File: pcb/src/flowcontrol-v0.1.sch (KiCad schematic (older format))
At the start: 30 parts, among them J1 Fan 1, J2 Fan 2, J3 Temp Sensor (10k Thermistor), J4 Temp Sensor (10k Thermistor), J5 Internal USB, J6 Molex 4 Pin, J7 4 Pin DRGB LED, SW1 K2-1102SP-C4SC-04, U1 PICO_RP2040, U2 CH340G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

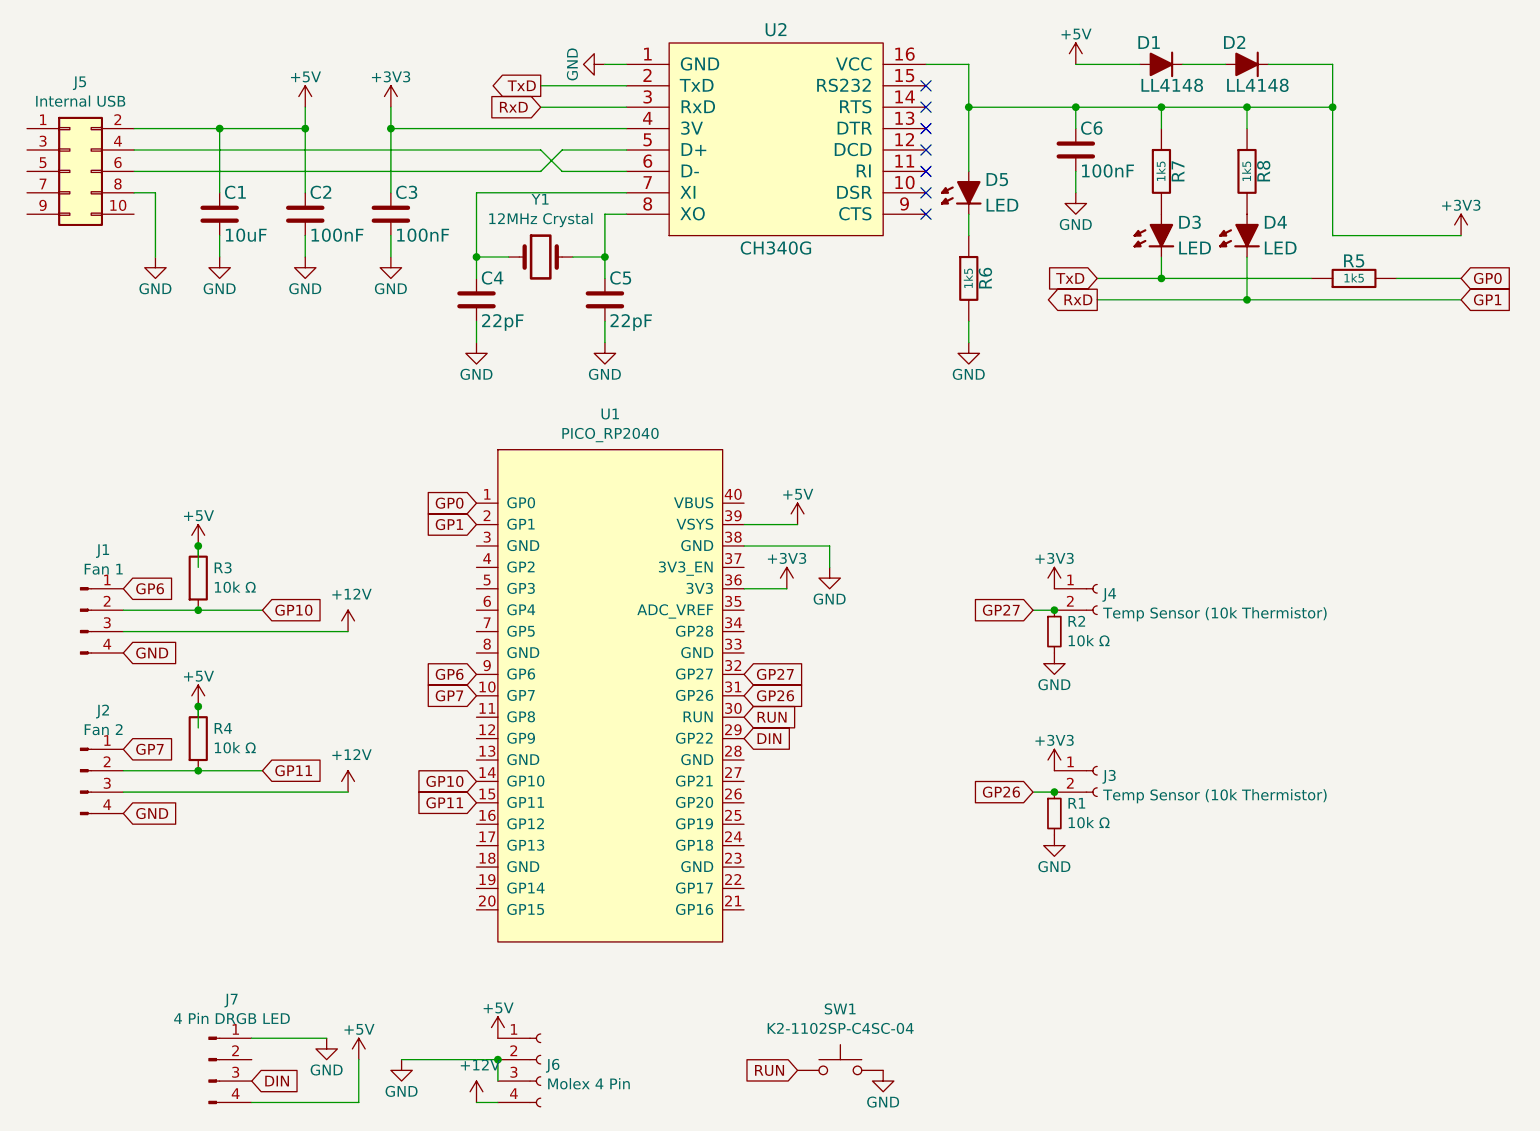
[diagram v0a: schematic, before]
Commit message: add revision 3 PCB (#47)
* add revision 3 PCB

* remove test firmwares
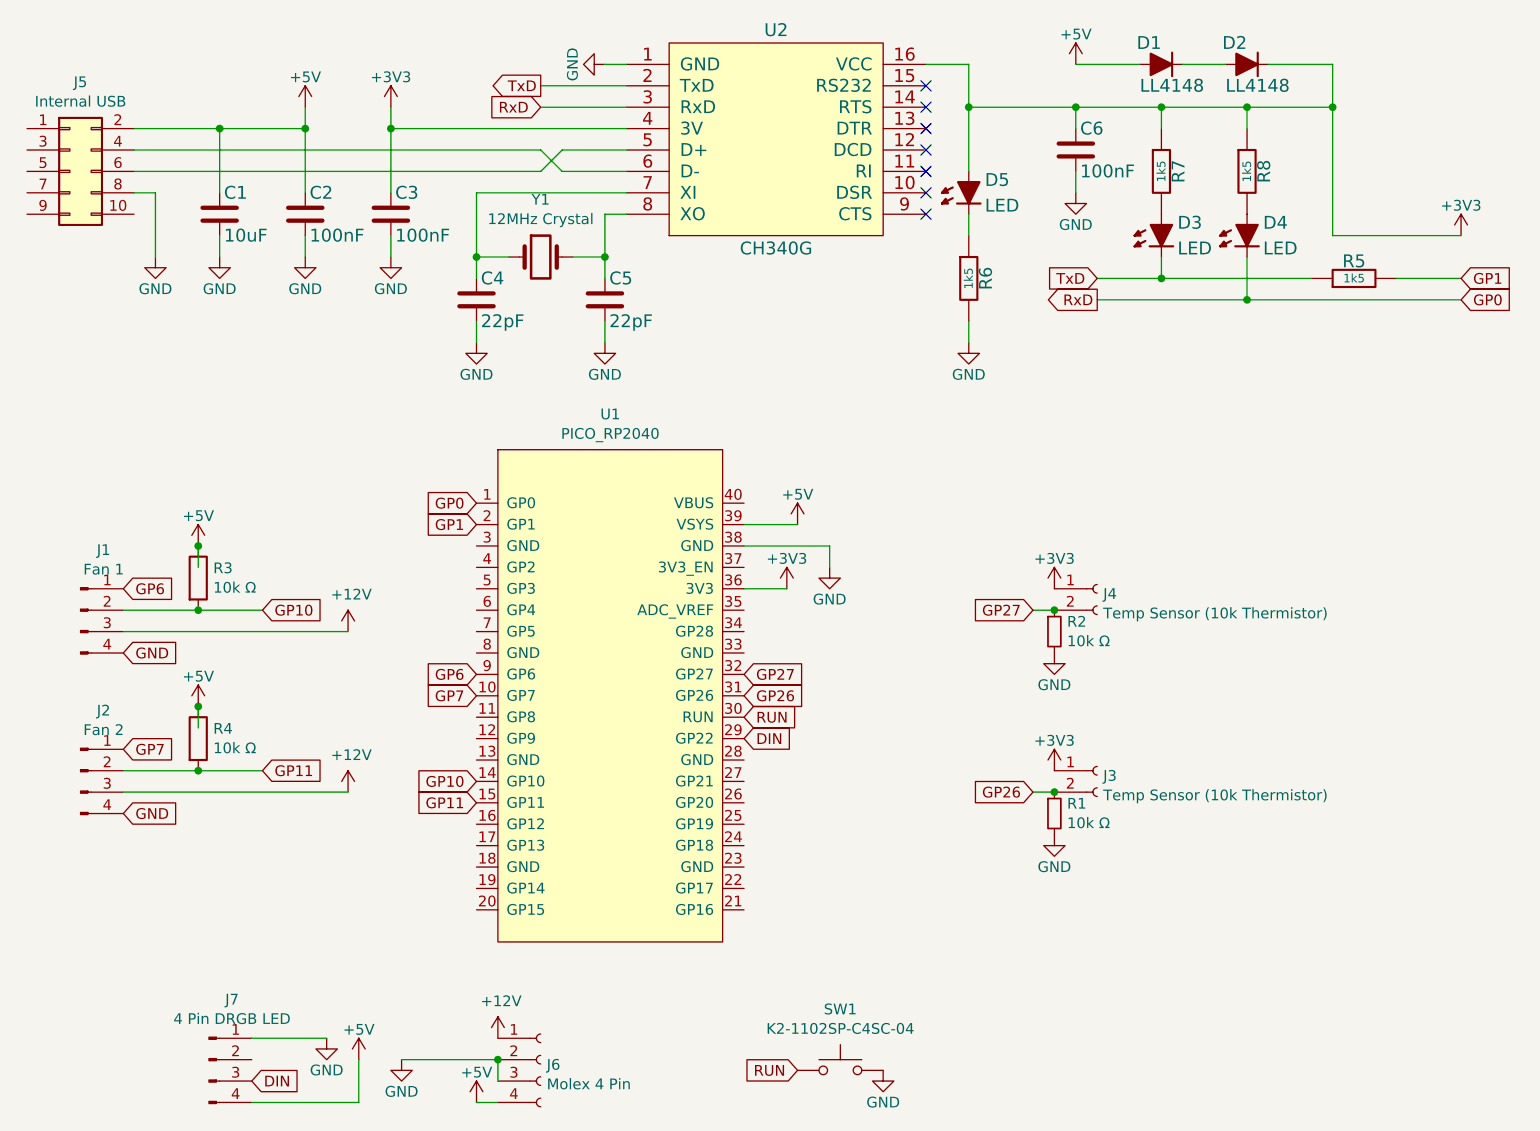
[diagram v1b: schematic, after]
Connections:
- net +12V: now also J6.1 (Pin_1); no longer J6.4 (Pin_4)
- net +5V: now also J6.4 (Pin_4); no longer J6.1 (Pin_1)
- net GP0: now also D4.1 (A), U2.3 (RxD); no longer R5.2
- net GP1: now also R5.2; no longer D4.1 (A), U2.3 (RxD)
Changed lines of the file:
@@
 Wire Wire Line
 	5650 3650 6050 3650
+Text GLabel 9000 2500 2    50   Input ~ 0
+GP0
 Text GLabel 9000 2400 2    50   Input ~ 0
-GP0
-Text GLabel 9000 2500 2    50   Input ~ 0
 GP1
 $Comp
@@
 L flowcontrol-v0.1-rescue:+5V-CH340G_D-SUN-V3.0-rescue #PWR0122
 U 1 1 60D932E4
-P 4500 5950
-F 0 "#PWR0122" H 4500 5800 50  0001 C CNN
-F 1 "+5V" H 4500 6090 50  0000 C CNN
-F 2 "" H 4500 5950 60  0000 C CNN
-F 3 "" H 4500 5950 60  0000 C CNN
-	1    4500 5950
+P 4400 6250
+F 0 "#PWR0122" H 4400 6100 50  0001 C CNN
+F 1 "+5V" H 4400 6390 50  0000 C CNN
+F 2 "" H 4400 6250 60  0000 C CNN
+F 3 "" H 4400 6250 60  0000 C CNN
+	1    4400 6250
 	1    0    0    -1
 $EndComp
@@
 L power:+12V #PWR0130
 U 1 1 60D76DB0
-P 4400 6250
-F 0 "#PWR0130" H 4400 6100 50  0001 C CNN
-F 1 "+12V" H 4415 6423 50  0000 C CNN
-F 2 "" H 4400 6250 50  0001 C CNN
-F 3 "" H 4400 6250 50  0001 C CNN
-	1    4400 6250
-	1    0    0    -1
-$EndComp
+P 4500 5950
+F 0 "#PWR0130" H 4500 5800 50  0001 C CNN
+F 1 "+12V" H 4515 6123 50  0000 C CNN
+F 2 "" H 4500 5950 50  0001 C CNN
+F 3 "" H 4500 5950 50  0001 C CNN
+	1    4500 5950
+	1    0    0    -1
+$EndComp
